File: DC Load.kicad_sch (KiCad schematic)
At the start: 158 parts, among them IC1 REF7050QDGKR, IC10 REF7050QDGKR, IC11 ISO7740FQDBQRQ1, IC12 ISO7741FQDBQRQ1, IC13 INA826AID, IC14 OPA210IDGKR, IC15 INA296A3IDDFR, IC16 MAX31850K, IC17 ISO7741FQDBQRQ1, IC18 ISO7741FQDBQRQ1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

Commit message: small changes
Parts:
- added J1: UI, 1190363:1190363, symbol 1190363:1190363
- J2: footprint Connector_PinSocket_2.54mm:PinSocket_1x06_P2.54mm_Vertical -> Connector_PinSocket_2.54mm:PinSocket_1x04_P2.54mm_Vertical; symbol Connector_Generic:Conn_01x06 -> Connector_Generic:Conn_01x04
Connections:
- net at A1.16 (D13/SCK): now also J2.4 (Pin_4); no longer J2.6 (Pin_6)
- net at A1.22 (A3): now also J2.3 (Pin_3); no longer J2.5 (Pin_5)
- net at A1.23 (SDA/A4): now also J2.2 (Pin_2); no longer J2.4 (Pin_4)
- net at A1.24 (SCL/A5): now also J2.1 (Pin_1); no longer J2.3 (Pin_3)
- net at A1.25 (A6): now also J1.1; no longer J2.2 (Pin_2)
- net at A1.26 (A7): now also J1.3; no longer J2.1 (Pin_1)
- no-connect marks 60 -> 63
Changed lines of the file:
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@@
 	)
 	(no_connect
+		(at 132.08 210.82)
+	)
+	(no_connect
 		(at 554.99 48.26)
 	)
@@
 	)
 	(no_connect
+		(at 179.07 181.61)
+	)
+	(no_connect
 		(at 458.47 27.94)
 	)
@@
 	)
 	(no_connect
+		(at 158.75 181.61)
+	)
+	(no_connect
 		(at 106.68 50.8)
 	)
@@
 	(wire
 		(pts
+			(xy 154.94 172.72) (xy 154.94 170.18)
+		)
+		(stroke
+			(width 0)
+			(type default)
+		)
+	)
+	(wire
+		(pts
 			(xy 452.12 207.01) (xy 452.12 217.17)
 		)
@@
 	(wire
 		(pts
+			(xy 190.5 152.4) (xy 190.5 166.37)
+		)
+		(stroke
+			(width 0)
+			(type default)
+		)
+	)
+	(wire
+		(pts
 			(xy 406.4 36.83) (xy 411.48 36.83)
 		)
@@
 	(wire
 		(pts
-			(xy 182.88 160.02) (xy 182.88 166.37)
-		)
-		(stroke
-			(width 0)
-			(type default)
-		)
-	)
-	(wire
-		(pts
 			(xy 502.92 50.8) (xy 505.46 50.8)
 		)
@@
 	(wire
 		(pts
+			(xy 156.21 168.91) (xy 156.21 184.15)
+		)
+		(stroke
+			(width 0)
+			(type default)
+		)
+	)
+	(wire
+		(pts
 			(xy 226.06 242.57) (xy 226.06 245.11)
 		)
@@
 	(wire
 		(pts
+			(xy 156.21 184.15) (xy 158.75 184.15)
+		)
+		(stroke
+			(width 0)
+			(type default)
+		)
+	)
+	(wire
+		(pts
 			(xy 473.71 195.58) (xy 473.71 191.77)
 		)
@@
 	(wire
 		(pts
+			(xy 185.42 157.48) (xy 185.42 166.37)
+		)
+		(stroke
+			(width 0)
+			(type default)
+		)
+	)
+	(wire
+		(pts
 			(xy 172.72 149.86) (xy 214.63 149.86)
 		)
@@
 	(wire
 		(pts
+			(xy 180.34 168.91) (xy 156.21 168.91)
+		)
+		(stroke
+			(width 0)
+			(type default)
+		)
+	)
+	(wire
+		(pts
 			(xy 486.41 217.17) (xy 486.41 215.9)
 		)
@@
 	(wire
 		(pts
-			(xy 187.96 154.94) (xy 187.96 166.37)
-		)
-		(stroke
-			(width 0)
-			(type default)
-		)
-	)
-	(wire
-		(pts
 			(xy 548.64 203.2) (xy 553.72 203.2)
 		)
@@
 	(wire
 		(pts
+			(xy 180.34 162.56) (xy 180.34 168.91)
+		)
+		(stroke
+			(width 0)
+			(type default)
+		)
+	)
+	(wire
+		(pts
 			(xy 425.45 167.64) (xy 438.15 167.64)
 		)
@@
 	(wire
 		(pts
-			(xy 190.5 152.4) (xy 190.5 166.37)
-		)
-		(stroke
-			(width 0)
-			(type default)
-		)
-	)
-	(wire
-		(pts
 			(xy 125.73 149.86) (xy 125.73 147.32)
 		)
@@
 	(wire
 		(pts
-			(xy 154.94 170.18) (xy 171.45 170.18)
+			(xy 154.94 172.72) (xy 144.78 172.72)
 		)
 		(stroke
@@
 	(wire
 		(pts
+			(xy 187.96 154.94) (xy 187.96 166.37)
+		)
+		(stroke
+			(width 0)
+			(type default)
+		)
+	)
+	(wire
+		(pts
 			(xy 213.36 255.27) (xy 222.25 255.27)
 		)
@@
 	(wire
 		(pts
+			(xy 182.88 160.02) (xy 182.88 184.15)
+		)
+		(stroke
+			(width 0)
+			(type default)
+		)
+	)
+	(wire
+		(pts
 			(xy 421.64 189.23) (xy 421.64 195.58)
 		)
@@
 	(wire
 		(pts
-			(xy 185.42 157.48) (xy 185.42 166.37)
-		)
-		(stroke
-			(width 0)
-			(type default)
-		)
-	)
-	(wire
-		(pts
 			(xy 224.79 287.02) (xy 224.79 288.29)
 		)
@@
 	(wire
 		(pts
+			(xy 182.88 184.15) (xy 179.07 184.15)
+		)
+		(stroke
+			(width 0)
+			(type default)
+		)
+	)
+	(wire
+		(pts
 			(xy 477.52 66.04) (xy 477.52 69.85)
 		)
@@
 	(wire
 		(pts
-			(xy 180.34 162.56) (xy 180.34 166.37)
-		)
-		(stroke
-			(width 0)
-			(type default)
-		)
-	)
-	(wire
-		(pts
 			(xy 497.84 113.03) (xy 509.27 113.03)
 		)
@@
 	(symbol
 		(lib_id "power:GND")
-		(at 171.45 170.18 0)
+		(at 144.78 172.72 0)
 		(unit 1)
 		(exclude_from_sim no)
@@
 		(fields_autoplaced yes)
 		(property "Reference" "#PWR03"
-			(at 171.45 176.53 0)
+			(at 144.78 179.07 0)
 			(effects
 				(font
@@
 		)
 		(property "Value" "GND"
-			(at 171.45 175.26 0)
+			(at 144.78 177.8 0)
 			(effects
 				(font
@@
 		)
 		(property "Footprint" ""
-			(at 171.45 170.18 0)
+			(at 144.78 172.72 0)
 			(effects
 				(font
@@
 		)
 		(property "Datasheet" ""
-			(at 171.45 170.18 0)
+			(at 144.78 172.72 0)
 			(effects
 				(font
@@
 		)
 		(property "Description" "Power symbol creates a global label with name \"GND\" , ground"
-			(at 171.45 170.18 0)
+			(at 144.78 172.72 0)
 			(effects
 				(font
@@
 	)
 	(symbol
+		(lib_id "1190363:1190363")
+		(at 179.07 184.15 180)
+		(unit 1)
+		(exclude_from_sim no)
+		(in_bom yes)
+		(on_board yes)
+		(dnp no)
+		(fields_autoplaced yes)
+		(property "Reference" "J1"
+			(at 168.91 191.77 0)
+			(effects
+				(font
+					(size 1.27 1.27)
+				)
+				(hide yes)
+			)
+		)
+		(property "Value" "UI"
+			(at 168.91 176.53 0)
+			(effects
+				(font
+					(size 1.27 1.27)
+				)
+			)
+		)
+		(property "Footprint" "1190363:1190363"
+			(at 162.56 89.23 0)
+			(effects
+				(font
+					(size 1.27 1.27)
+				)
+				(justify left top)
+				(hide yes)
+			)
+		)
+		(property "Datasheet" "http://www.phoenixcontact.net/product/1190363"
+			(at 162.56 -10.77 0)
+			(effects
+				(font
+					(size 1.27 1.27)
+				)
+				(justify left top)
+				(hide yes)
+			)
+		)
+		(property "Description" "PCB terminal block, nominal current: 24 A, number of potentials: 2, Solder pin [P]: 3.5 mm."
+			(at 179.07 184.15 0)
+			(effects
+				(font
+					(size 1.27 1.27)
+				)
+				(hide yes)
+			)
+		)
+		(property "Height" "20.28"
+			(at 162.56 -210.77 0)
+			(effects
+				(font
+					(size 1.27 1.27)
+				)
+				(justify left top)
+				(hide yes)
+			)
+		)
+		(property "Mouser Part Number" "651-1190363"
+			(at 162.56 -310.77 0)
+			(effects
+				(font
+					(size 1.27 1.27)
+				)
+				(justify left top)
+				(hide yes)
+			)
+		)
+		(property "Mouser Price/Stock" "https://www.mouser.co.uk/ProductDetail/Phoenix-Contact/1190363?qs=QNEnbhJQKvZM1o20TNh%252B9Q%3D%3D"
+			(at 162.56 -410.77 0)
+			(effects
+				(font
+					(size 1.27 1.27)
+				)
+				(justify left top)
+				(hide yes)
+			)
+		)
+		(property "Manufacturer_Name" "Phoenix Contact"
+			(at 162.56 -510.77 0)
+			(effects
+				(font
+					(size 1.27 1.27)
+				)
+				(justify left top)
+				(hide yes)
+			)
+		)
+		(property "Manufacturer_Part_Number" "1190363"
+			(at 162.56 -610.77 0)
+			(effects
+				(font
+					(size 1.27 1.27)
+				)
+				(justify left top)
+				(hide yes)
+			)
+		)
+		(pin "2"
+		)
+		(pin "3"
+		)
+		(pin "4"
+		)
+		(pin "1"
+		)
+		(instances
+			(project "DC Load"
+				(path "/9c244068-8ef8-45bd-bef5-5ed489349933"
+					(reference "J1")
+					(unit 1)
+				)
+			)
+		)
+	)
+	(symbol
 		(lib_id "L78L06ACD13TR:L78L06ACD13TR")
 		(at 400.05 276.86 0)
@@
 	)
 	(symbol
-		(lib_id "Connector_Generic:Conn_01x06")
-		(at 185.42 171.45 90)
+		(lib_id "Connector_Generic:Conn_01x04")
+		(at 187.96 171.45 90)
 		(mirror x)
 		(unit 1)
@@
 		(dnp no)
 		(property "Reference" "J2"
-			(at 184.1499 173.99 0)
+			(at 186.6899 173.99 0)
 			(effects
 				(font
@@
 		)
 		(property "Value" "Conn_01x06"
-			(at 186.6899 173.99 0)
+			(at 189.2299 173.99 0)
 			(effects
 				(font
@@
 			)
 		)
-		(property "Footprint" "Connector_PinSocket_2.54mm:PinSocket_1x06_P2.54mm_Vertical"
-			(at 185.42 171.45 0)
+		(property "Footprint" "Connector_PinSocket_2.54mm:PinSocket_1x04_P2.54mm_Vertical"
+			(at 187.96 171.45 0)
 			(effects
 				(font
@@
 		)
 		(property "Datasheet" "~"
-			(at 185.42 171.45 0)
+			(at 187.96 171.45 0)
 			(effects
 				(font
@@
 			)
 		)
-		(property "Description" "Generic connector, single row, 01x06, script generated (kicad-library-utils/schlib/autogen/connector/)"
-			(at 185.42 171.45 0)
+		(property "Description" "Generic connector, single row, 01x04, script generated (kicad-library-utils/schlib/autogen/connector/)"
+			(at 187.96 171.45 0)
 			(effects
 				(font
@@
 		(pin "4"
 		)
-		(pin "5"
-		)
 		(pin "1"
 		)
 		(pin "3"
 		)
-		(pin "6"
-		)
 		(instances

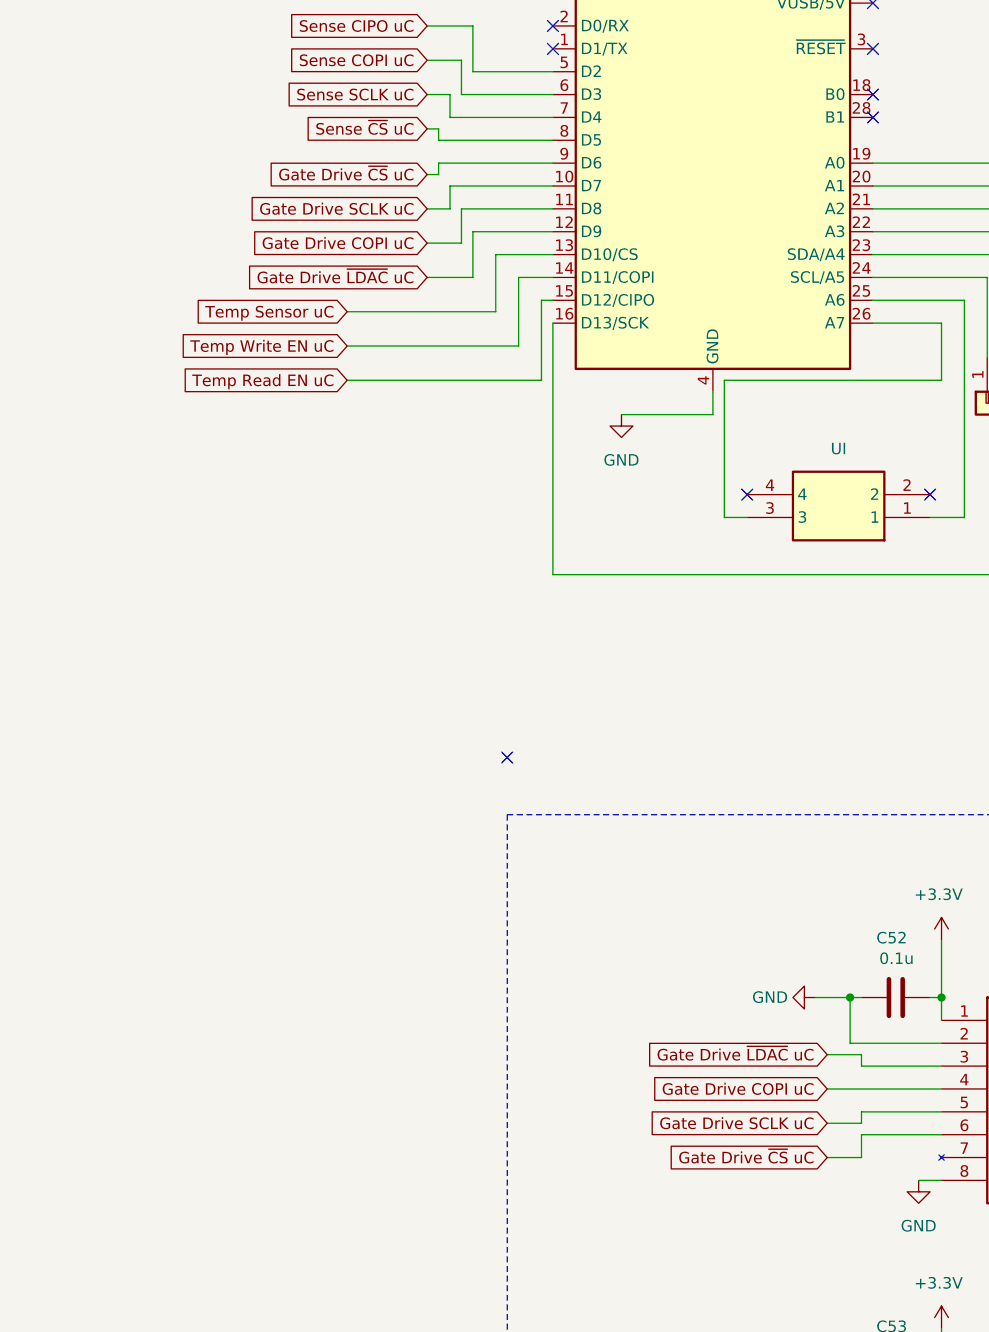
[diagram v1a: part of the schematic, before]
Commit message: fixed net names for DAC communincation
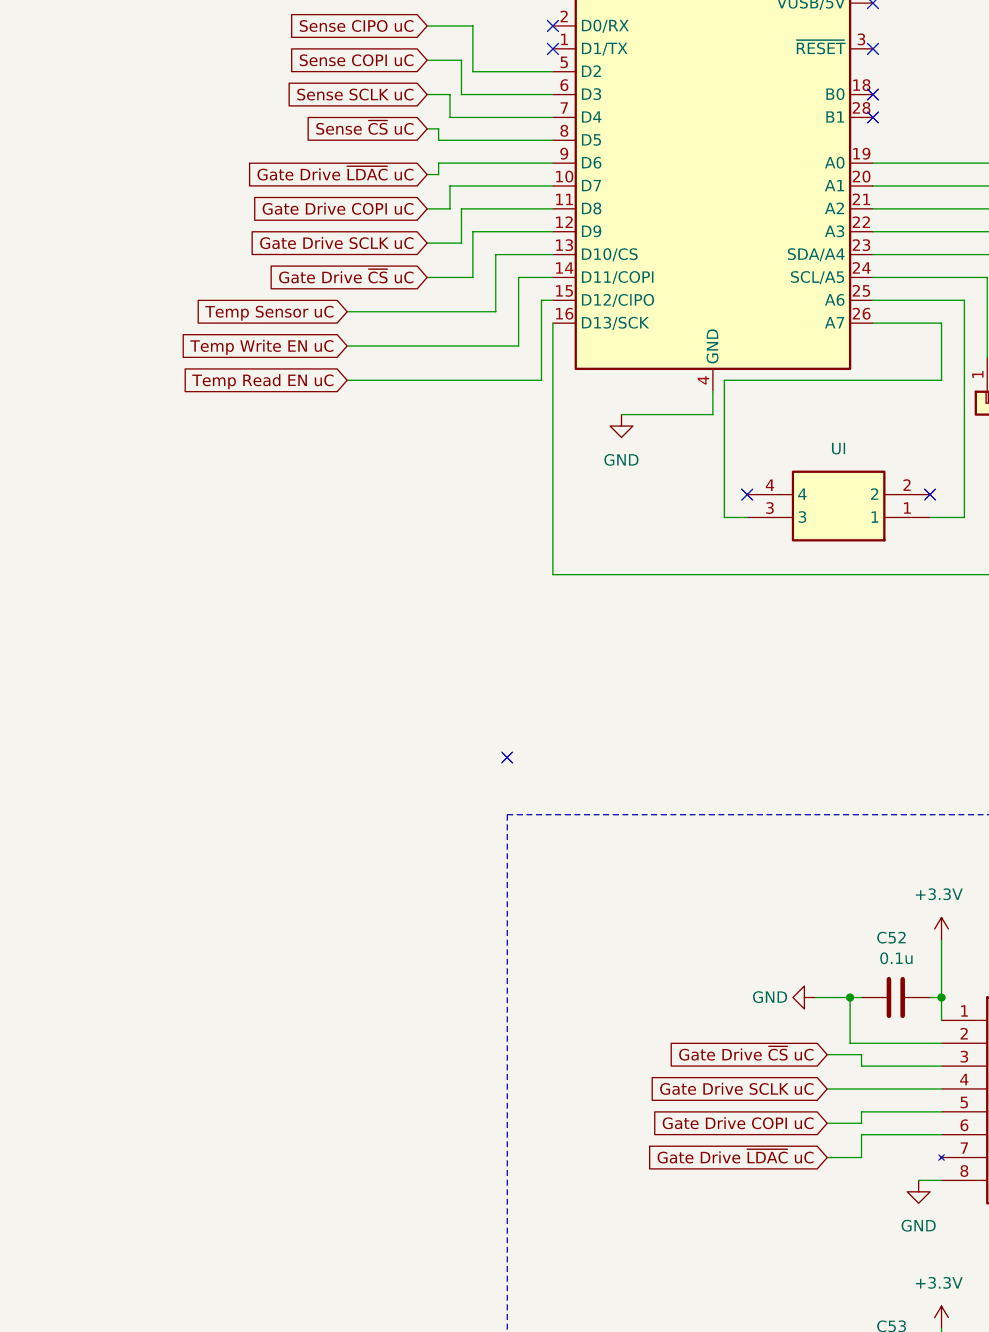
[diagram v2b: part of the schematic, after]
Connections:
- net Gate Drive COPI uC: now also A1.10 (D7), IC11.5 (INC); no longer A1.11 (D8), IC11.4 (INB)
- net Gate Drive SCLK uC: now also A1.11 (D8), IC11.4 (INB); no longer A1.10 (D7), IC11.5 (INC)
- net Gate Drive ~{CS} uC: now also A1.12 (D9), IC11.3 (INA); no longer A1.9 (D6), IC11.6 (IND)
- net Gate Drive ~{LDAC} uC: now also A1.9 (D6), IC11.6 (IND); no longer A1.12 (D9), IC11.3 (INA)
